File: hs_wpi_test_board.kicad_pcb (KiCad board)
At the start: 2 copper layers, 74.9 x 44.4 mm, 35 parts, among them J1 Raspberry_Pi_2_3, Q1 Q_NPN_EBC, Q10 Q_NPN_EBC, Q2 Q_NPN_EBC, Q3 Q_NPN_EBC, Q4 Q_NPN_EBC, Q5 Q_NPN_EBC, Q6 Q_NPN_EBC, Q7 Q_NPN_EBC, Q8 Q_NPN_EBC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

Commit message: update text on silkscreen
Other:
- board text added: "https://github.com/ppelleti/hs-wiringPi-test-board Patrick Pelletier 2017-08-08"
- board text removed: "https://hackage.haskell.org/package/wiringPi Patrick Pelletier 2017-08-07"
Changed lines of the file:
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@@
   )
   (page USLetter)
+  (title_block
+    (title "Test board for wiringPi Haskell binding")
+    (date 2017-08-08)
+    (company "Patrick Pelletier")
+  )
   (layers
     (0 F.Cu signal)
@@
     (effects (font (size 1.5 1.5) (thickness 0.3)))
   )
-  (gr_text "https://hackage.haskell.org/package/wiringPi   Patrick Pelletier 2017-08-07" (at 133.35 94.615) (layer B.SilkS)
+  (gr_text "https://github.com/ppelleti/hs-wiringPi-test-board   Patrick Pelletier 2017-08-08" (at 133.35 94.615) (layer B.SilkS)
     (effects (font (size 1 1) (thickness 0.25)) (justify mirror))
   )

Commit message: add KiCad and OSHW logos to back silkscreen
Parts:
- added REF***: OSHW-Logo_5.7x6mm_SilkScreen, Symbols:OSHW-Logo_5.7x6mm_SilkScreen, B.Cu at (165.7, 104.1)
- added REF***: KiCad-Logo2_6mm_SilkScreen, Symbols:KiCad-Logo2_6mm_SilkScreen, B.Cu at (151.8, 108.6)

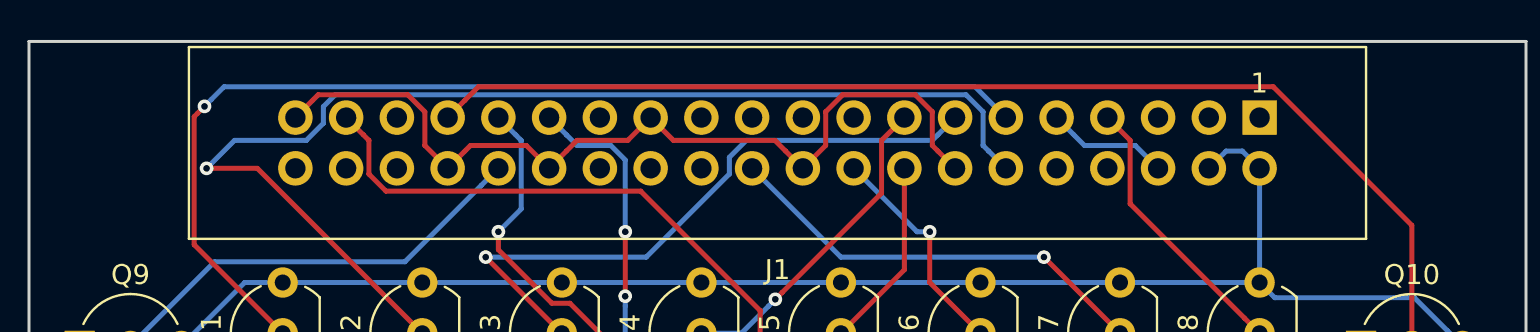
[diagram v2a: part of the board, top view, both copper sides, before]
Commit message: more drawings on silkscreen to indicate position of J1
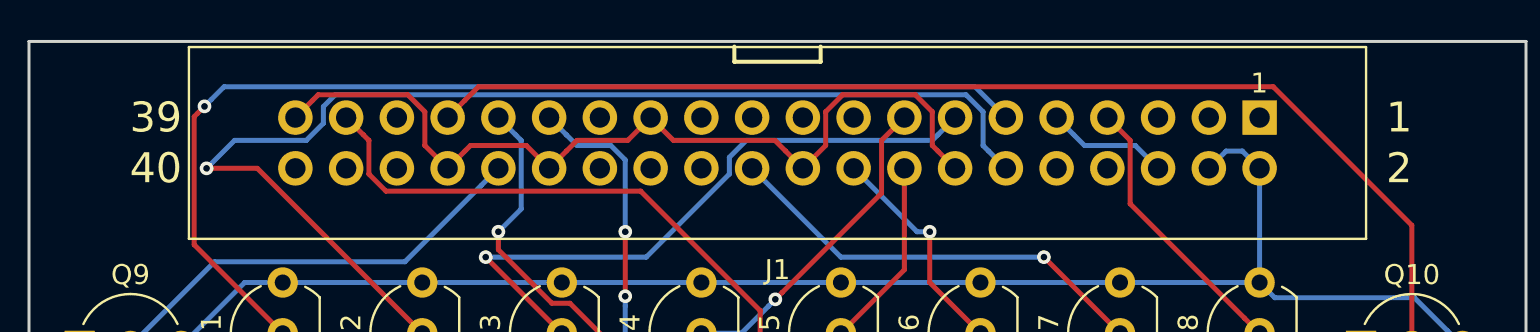
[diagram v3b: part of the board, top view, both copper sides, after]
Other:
- board text added: "1"
- board text added: "2"
- board text added: "39"
- board text added: "40"
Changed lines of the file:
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@@
     (links 65)
     (no_connects 0)
-    (area 96.444999 72.5896 171.525001 120.8124)
+    (area 96.444999 72.5896 177.68502 120.8124)
     (thickness 1.6)
-    (drawings 10)
+    (drawings 17)
     (tracks 252)
     (zones 0)
@@
       (xy -2.537313 2.939947) (xy -2.454562 2.96715) (xy -2.376928 2.977424) (xy -2.273043 2.973429)) (layer B.SilkS) (width 0.01))
   )
+  (gr_line (start 136.144 75.946) (end 136.144 75.184) (angle 90) (layer F.SilkS) (width 0.2))
+  (gr_line (start 131.826 75.946) (end 136.144 75.946) (angle 90) (layer F.SilkS) (width 0.2))
+  (gr_line (start 131.826 75.184) (end 131.826 75.946) (angle 90) (layer F.SilkS) (width 0.2))
+  (gr_text 40 (at 102.87 81.28) (layer F.SilkS)
+    (effects (font (size 1.5 1.5) (thickness 0.3)))
+  )
+  (gr_text 39 (at 102.87 78.74) (layer F.SilkS)
+    (effects (font (size 1.5 1.5) (thickness 0.3)))
+  )
+  (gr_text 2 (at 165.1 81.28) (layer F.SilkS)
+    (effects (font (size 1.5 1.5) (thickness 0.3)))
+  )
+  (gr_text 1 (at 165.1 78.74) (layer F.SilkS)
+    (effects (font (size 1.5 1.5) (thickness 0.3)))
+  )
   (gr_text "Test board\nfor wiringPi\nHaskell binding" (at 102.235 109.855 90) (layer F.SilkS)

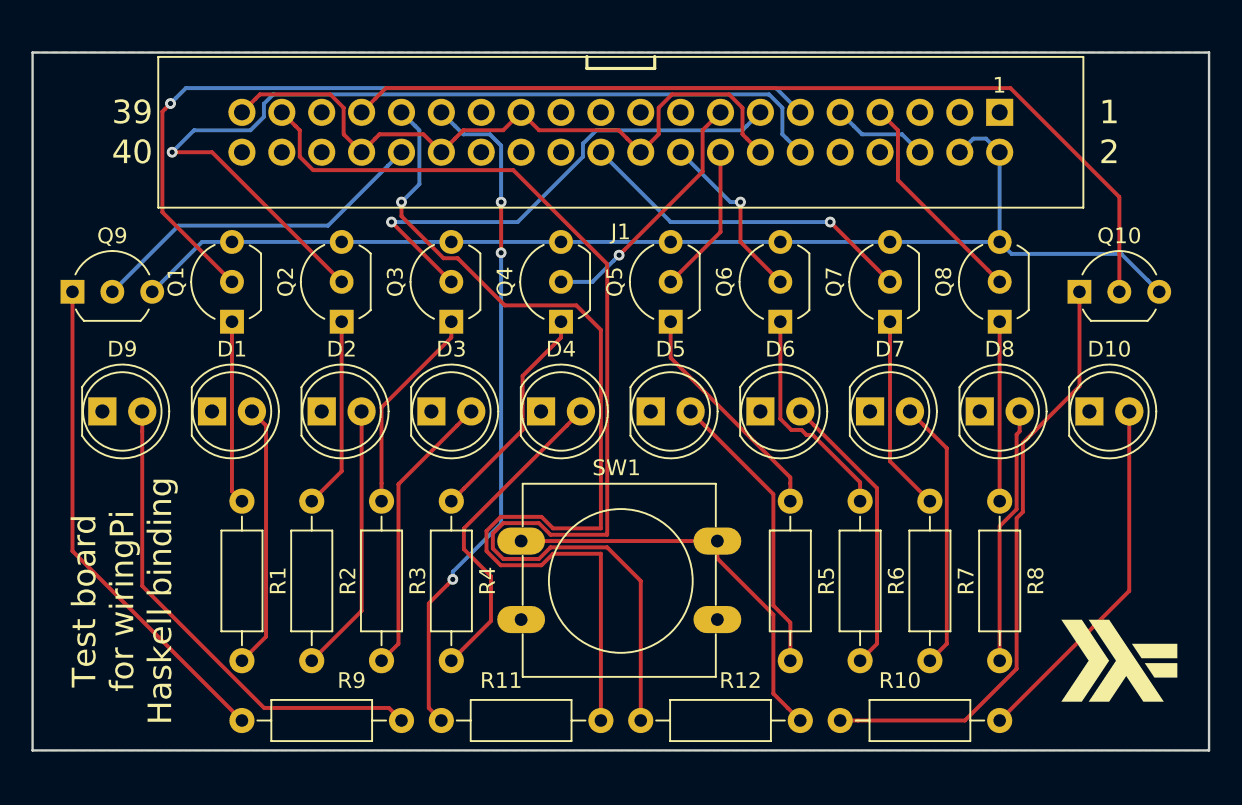
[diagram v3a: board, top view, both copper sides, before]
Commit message: use new button footprint
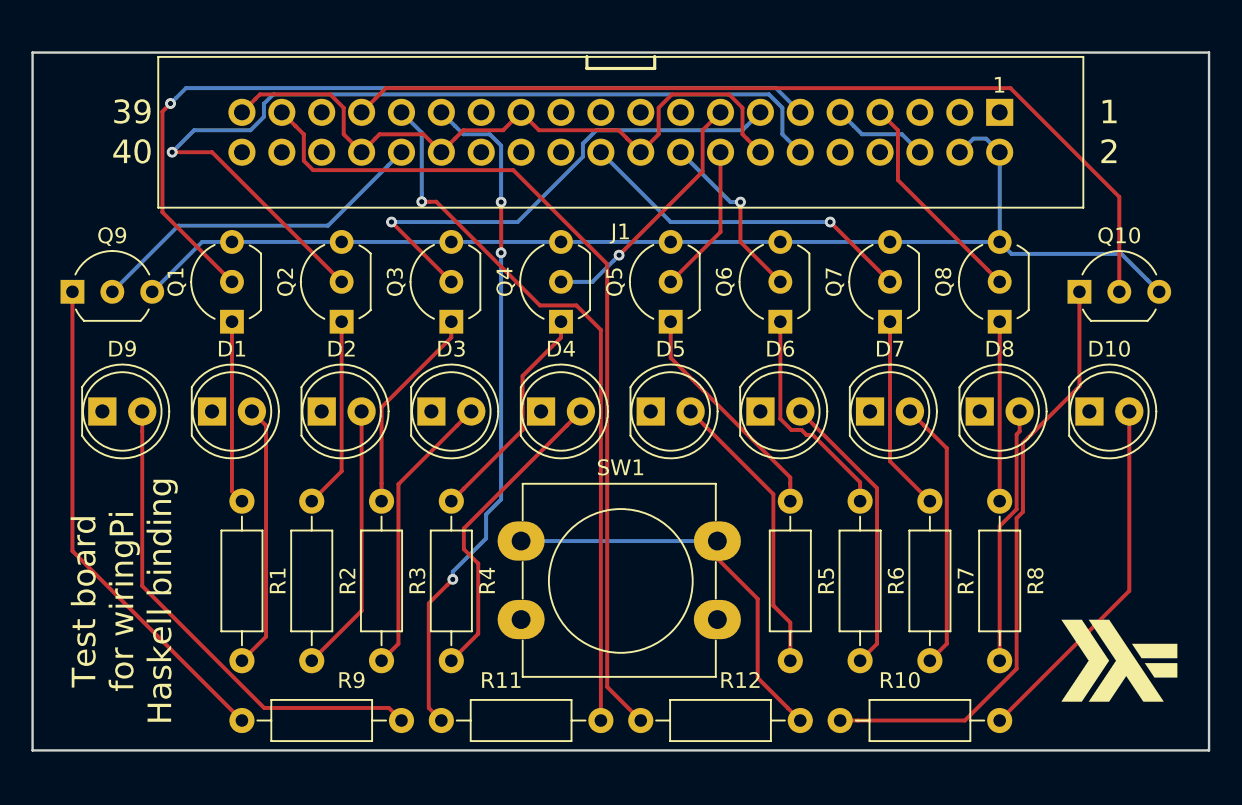
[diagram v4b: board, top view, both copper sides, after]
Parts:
- SW1: footprint Buttons_Switches_THT:SW_PUSH-12mm -> hs_wpi_test_board:SW_PUSH-12mm_Wurth-430476085716
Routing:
- net Net-(J1-Pad31): track 63.7 -> 45.9 mm
- net /Button: track 71.5 -> 55.7 mm
- net Net-(D4-Pad2): track 20.7 -> 20.1 mm
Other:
- board text added: "https://github.com/ppelleti/hs-wiringPi-test-board Patrick Pelletier 2017-08-22"
- board text removed: "https://github.com/ppelleti/hs-wiringPi-test-board Patrick Pelletier 2017-08-08"

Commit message: make board a little larger
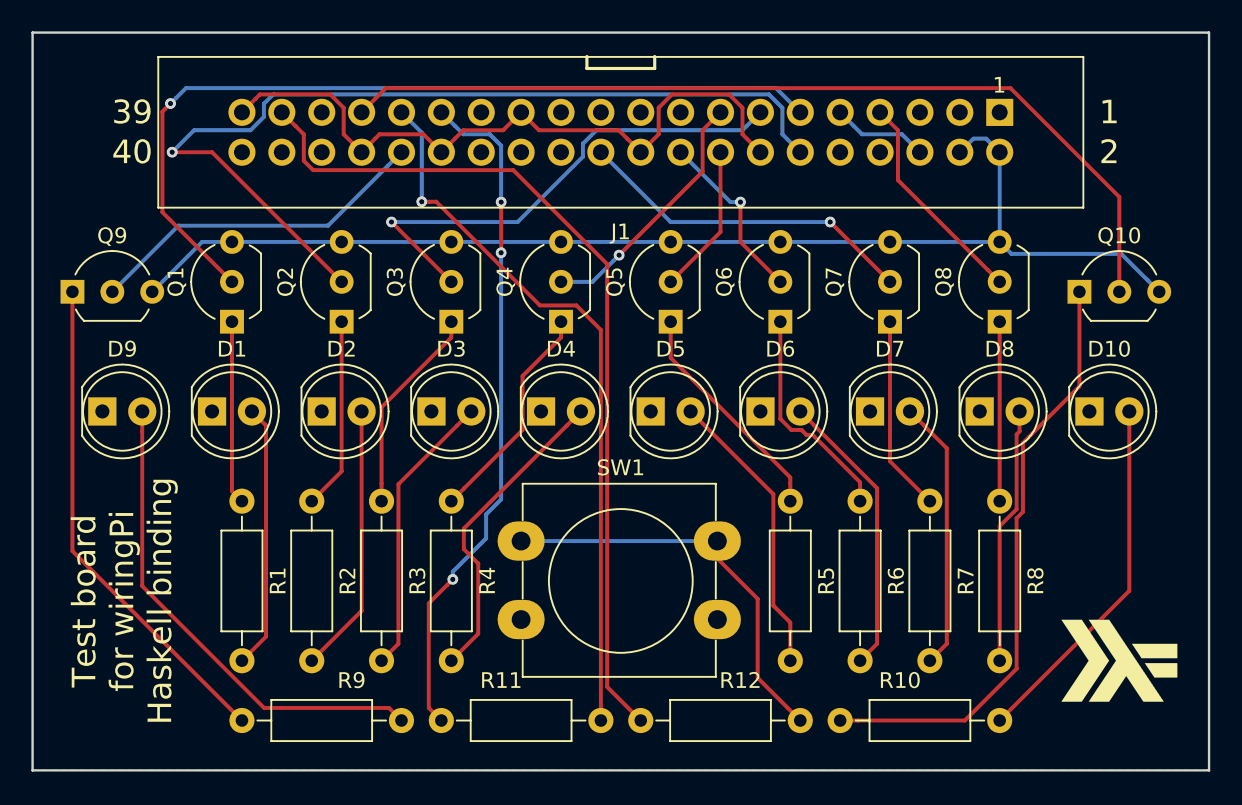
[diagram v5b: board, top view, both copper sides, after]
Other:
- board size 74.9 x 44.4 mm -> 74.9 x 47 mm
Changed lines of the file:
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@@
     )
   )
+  (gr_line (start 171.45 73.66) (end 96.52 73.66) (angle 90) (layer Edge.Cuts) (width 0.15))
+  (gr_line (start 171.45 120.65) (end 171.45 73.66) (angle 90) (layer Edge.Cuts) (width 0.15))
+  (gr_line (start 96.52 120.65) (end 171.45 120.65) (angle 90) (layer Edge.Cuts) (width 0.15))
+  (gr_line (start 96.52 73.66) (end 96.52 120.65) (angle 90) (layer Edge.Cuts) (width 0.15))
   (gr_line (start 136.144 75.946) (end 136.144 75.184) (angle 90) (layer F.SilkS) (width 0.2))
   (gr_line (start 131.826 75.946) (end 136.144 75.946) (angle 90) (layer F.SilkS) (width 0.2))
@@
     (effects (font (size 1 1) (thickness 0.25)) (justify mirror))
   )
-  (gr_line (start 96.52 119.38) (end 96.52 74.93) (angle 90) (layer Edge.Cuts) (width 0.15))
-  (gr_line (start 171.45 119.38) (end 96.52 119.38) (angle 90) (layer Edge.Cuts) (width 0.15))
-  (gr_line (start 171.45 74.93) (end 171.45 119.38) (angle 90) (layer Edge.Cuts) (width 0.15))
-  (gr_line (start 96.52 74.93) (end 171.45 74.93) (angle 90) (layer Edge.Cuts) (width 0.15))
   (gr_circle (center 165.735 113.665) (end 170.815 113.665) (layer B.SilkS) (width 1))
   (gr_circle (center 102.235 80.645) (end 107.315 80.645) (layer B.SilkS) (width 1))
@@
     (polygon
       (pts
-        (xy 171.45 119.38) (xy 96.52 119.38) (xy 96.52 74.93) (xy 171.45 74.93)
+        (xy 171.45 120.65) (xy 96.52 120.65) (xy 96.52 73.66) (xy 171.45 73.66)
       )
     )

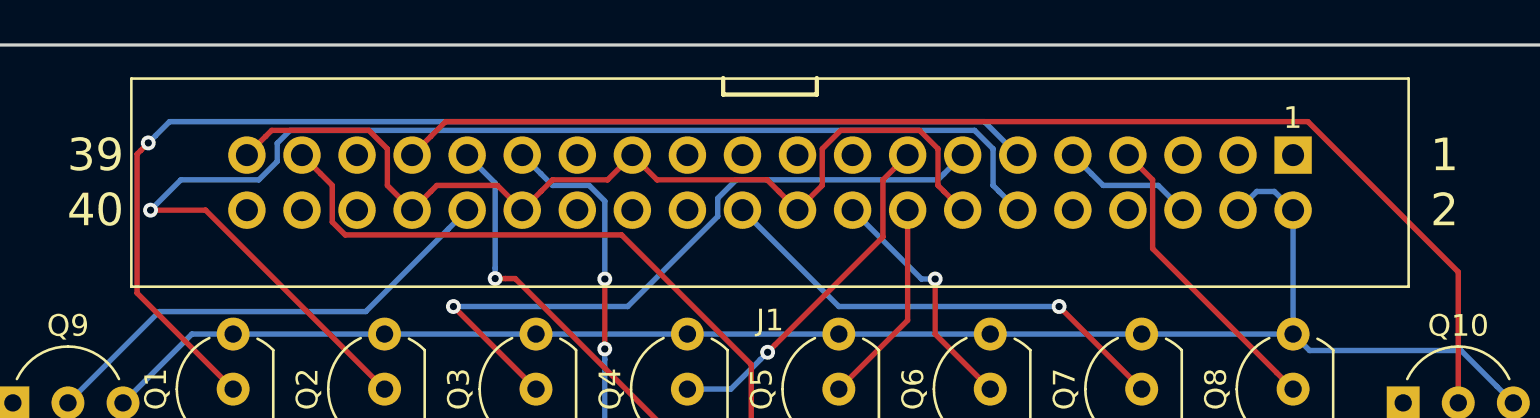
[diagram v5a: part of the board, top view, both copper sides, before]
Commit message: use connector footprint with notch on silkscreen
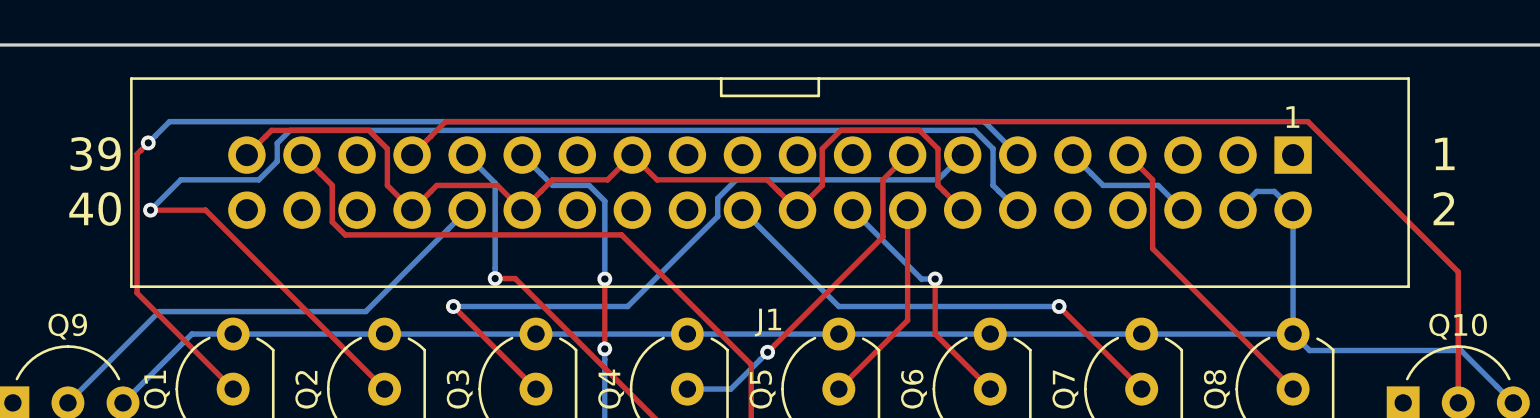
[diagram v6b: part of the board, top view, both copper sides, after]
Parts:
- J1: footprint Connectors:IDC_Header_Straight_40pins -> hs_wpi_test_board:IDC_Header_Straight_40pins_key
